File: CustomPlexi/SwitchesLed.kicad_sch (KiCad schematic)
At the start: 16 parts, among them SW1 Boost Enable/Disable, SW1 Plexi Channel Select, SW1 SW_SP3T, SW2 Clipping Type Select, SW4 Pedal Enable, SW6 Preamp Enable

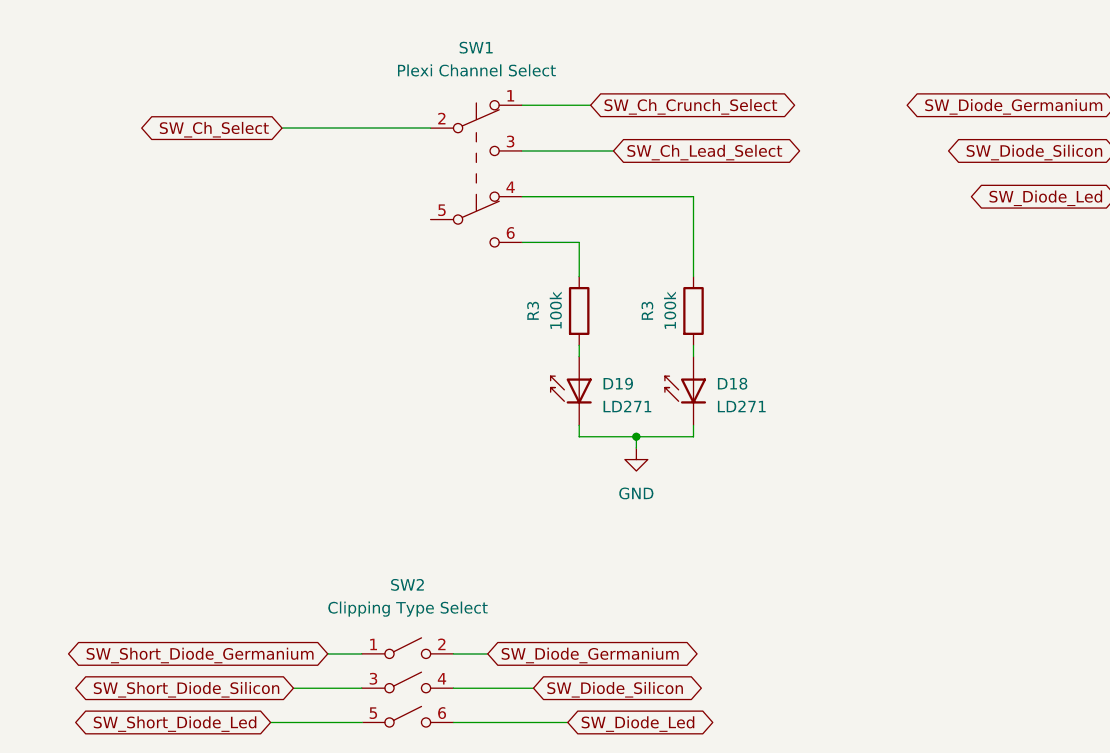
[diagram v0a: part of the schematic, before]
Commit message: added leds
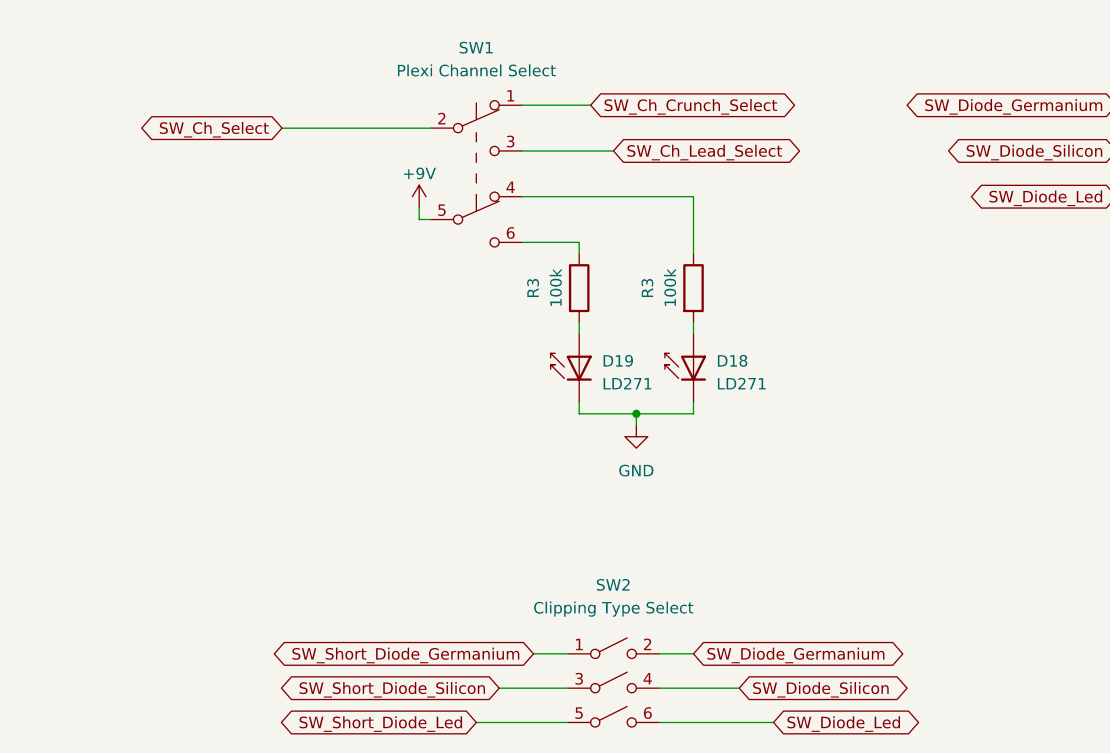
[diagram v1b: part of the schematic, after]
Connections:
- net +9V: now also SW1.5 (B)
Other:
- moved on the sheet: D18, D19, R3, SW2

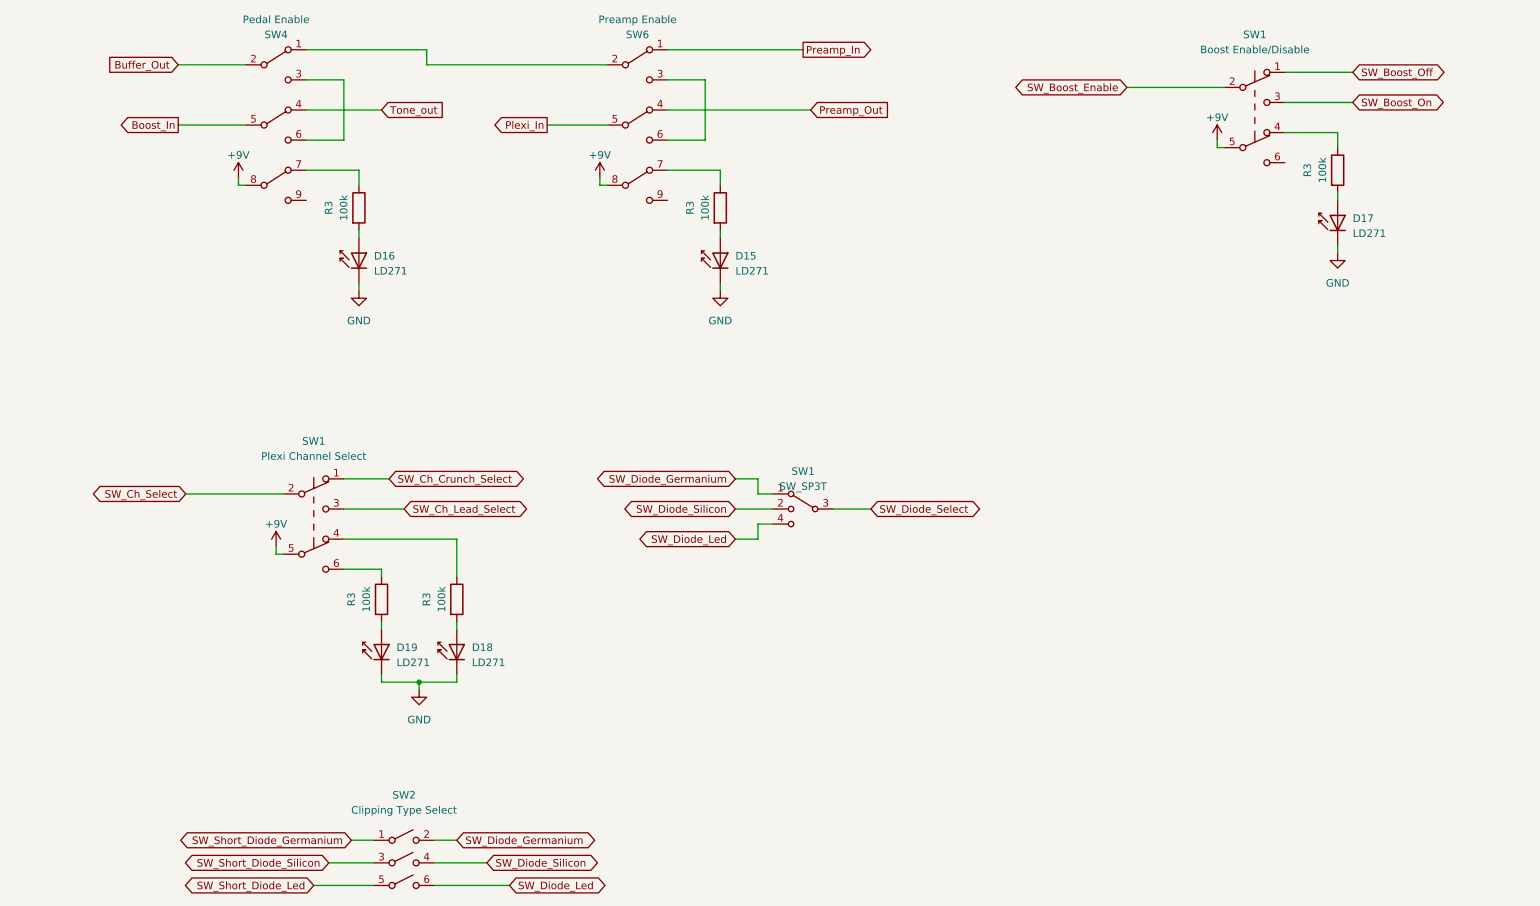
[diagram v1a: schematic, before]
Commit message: crunch and leadh channel has separated level control
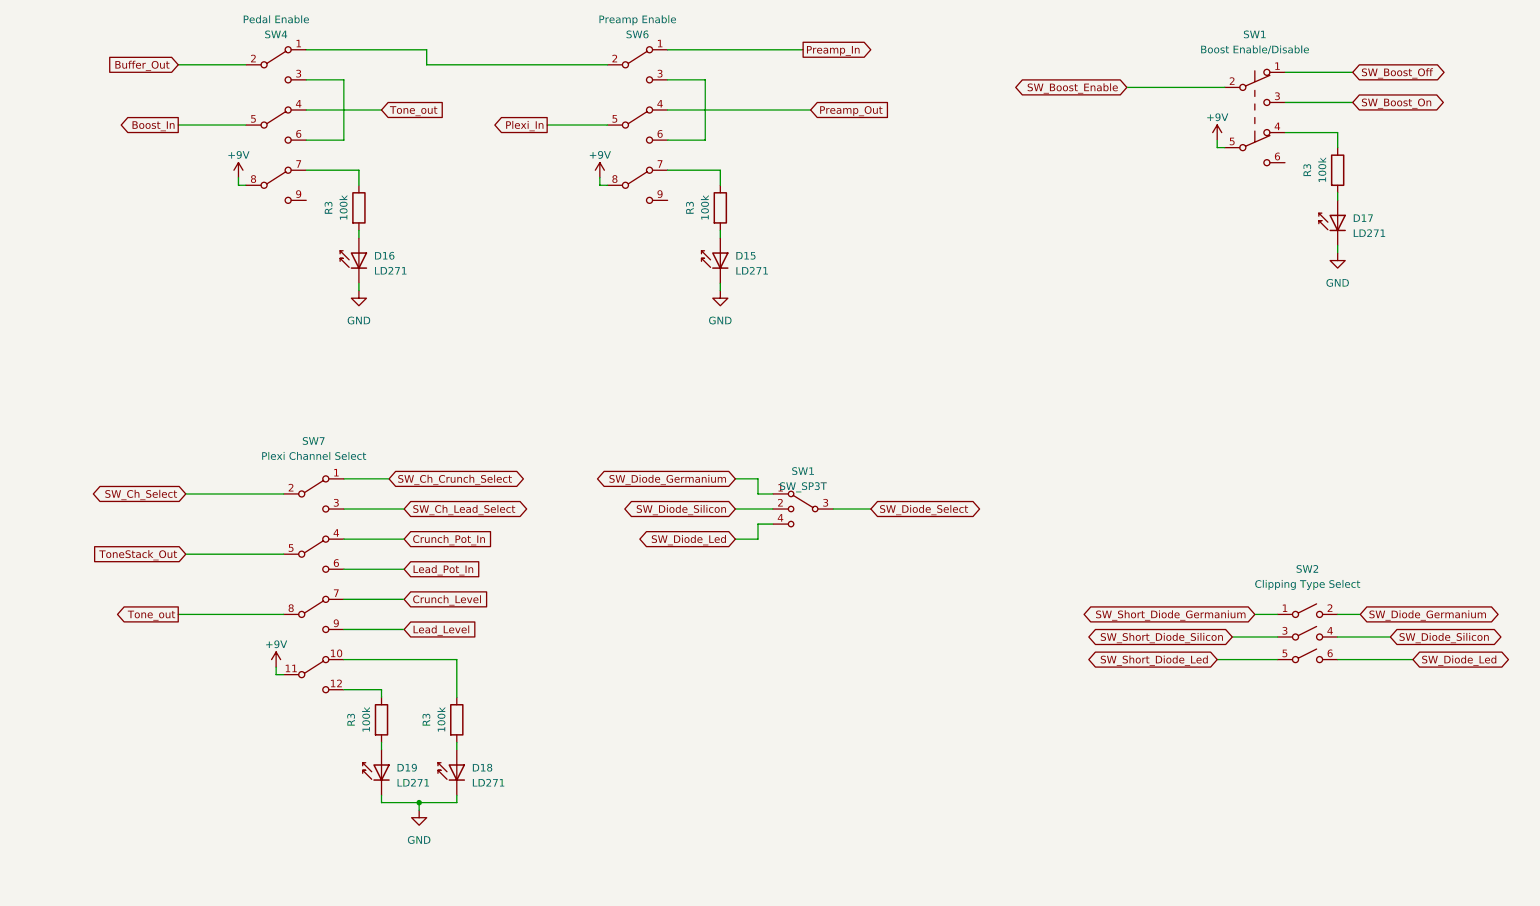
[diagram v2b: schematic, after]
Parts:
- removed SW1: Plexi Channel Select, symbol Switch:SW_Push_DPDT
- added SW7: Plexi Channel Select, symbol CustomLib:SW_4PDT
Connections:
- net +9V: now also SW7.11
- net SW_Ch_Crunch_Select: now also SW7.1
- net SW_Ch_Lead_Select: now also SW7.3
- net SW_Ch_Select: now also SW7.2
- net Tone_out: now also SW7.8
- net at R3.1: now also SW7.12
- net at R3.1: now also SW7.10
- new net Crunch_Level: SW7.7
- new net Crunch_Pot_In: SW7.4
- new net Lead_Level: SW7.9
- new net Lead_Pot_In: SW7.6
- new net ToneStack_Out: SW7.5
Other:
- moved on the sheet: D18, D19, R3, SW2

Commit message: some changes
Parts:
- removed D17: LD271, LED_THT:LED_D5.0mm_IRGrey, symbol LED:LD271
- removed R3: 100k, Resistor_SMD_AKL:R_0603_1608Metric, symbol PCM_Resistor_AKL:R_0603
- removed SW1: SW_SP3T, symbol Switch:SW_SP3T
- removed SW1: Boost Enable/Disable, symbol Switch:SW_Push_DPDT
- removed SW2: Clipping Type Select, symbol CustomLib:SW_3PST

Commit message: commit
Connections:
- net at SW6.2: no longer SW4.1
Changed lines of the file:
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@@
-    (stroke (width 0) (type default))
-  )
-  (wire (pts (xy 86.36 34.29) (xy 116.84 34.29))
     (stroke (width 0) (type default))
   )
